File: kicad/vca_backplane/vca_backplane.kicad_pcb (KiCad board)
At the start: 4 copper layers, 147.2 x 109.9 mm, 102 parts, among them J1 Conn_02x20_Odd_Even, J10 AudioJack3DPDT, J2 Eurorack Power, J3 Conn_02x20_Odd_Even, J4 Conn_02x20_Odd_Even, J5 Conn_02x20_Odd_Even, J6 Conn_02x20_Odd_Even, J7 Conn_02x20_Odd_Even, J8 Conn_02x20_Odd_Even, J9 AudioJack3DPDT, Q1 DMMT5401, Q2 DMG2305UX, Q3 BSS138, Q4 BSS138, U1 74HCT138, U10 NE5532, U11 74HCT138, U12 MAX333A, U13 MAX333A, U14 NE5532, U2 74HCT245, U3 74LVC245, U4 MCP4822, U5 PCA9555PW, U7 AS3360, U8 M24C02-WMN, U9 PS508

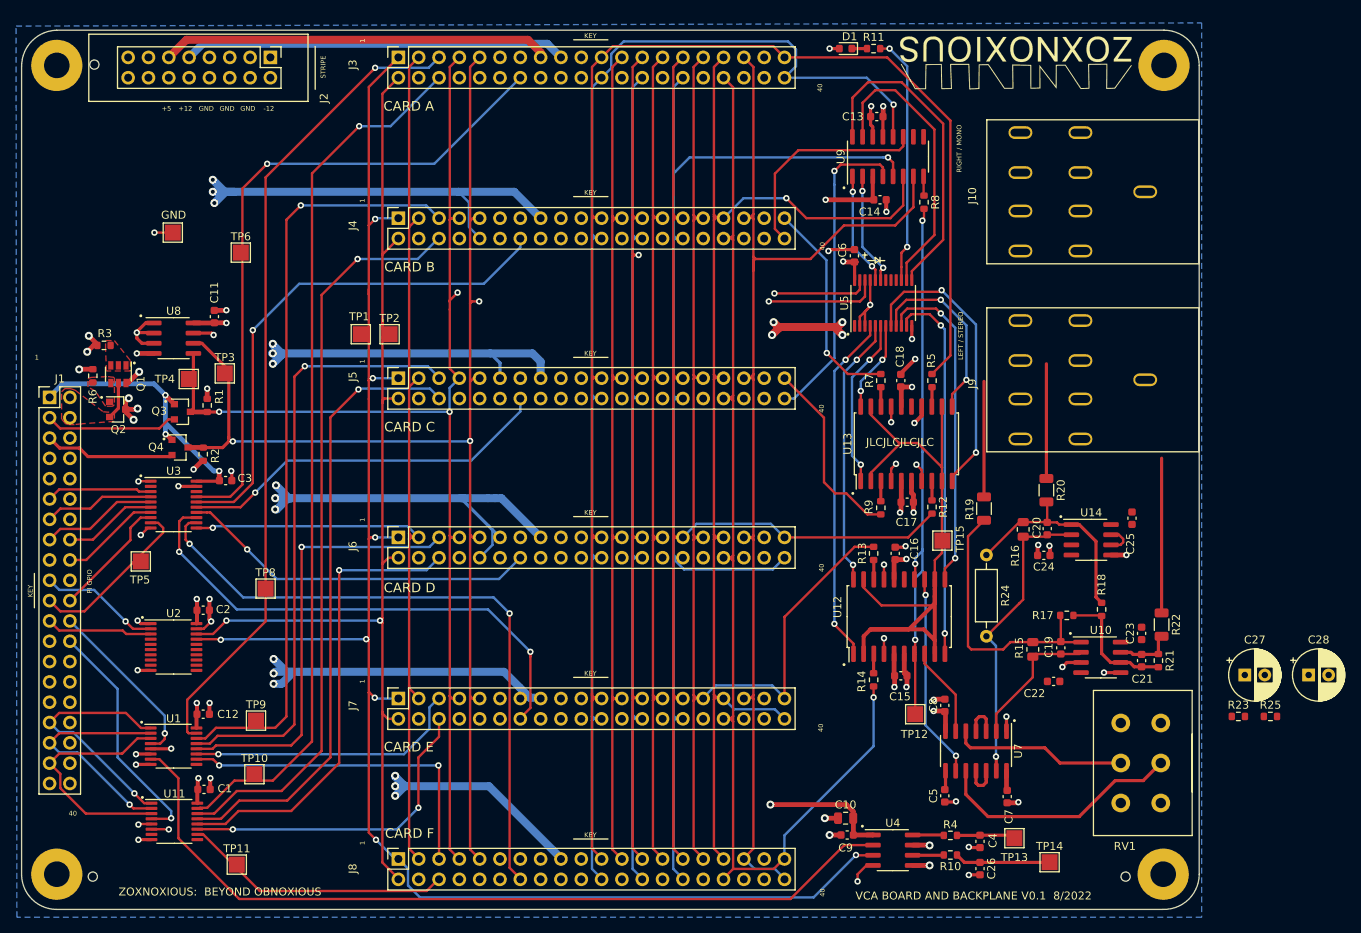
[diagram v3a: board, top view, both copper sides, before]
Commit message: fix some poor routing
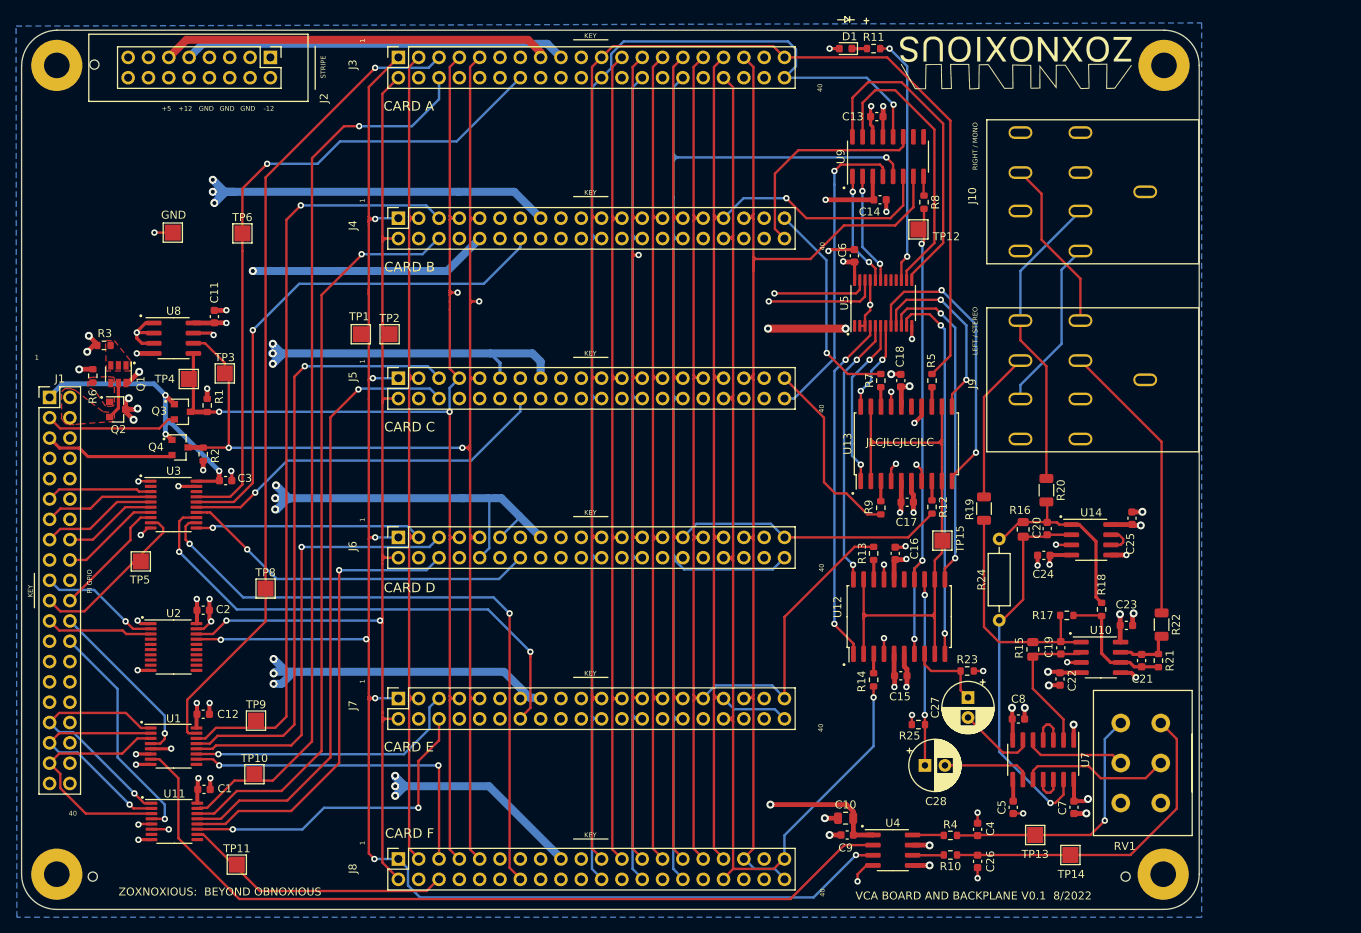
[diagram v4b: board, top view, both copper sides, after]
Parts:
- moved TP12 60.6 mm to (142.0, 58.3)
- moved C28 49.3 mm to (142.8, 125.3)
- moved R25 44.0 mm to (142.0, 120.2), turned to 180 degrees
- moved C27 34.7 mm to (148.2, 116.8), turned to -90 degrees
- moved R23 34.4 mm to (148.1, 113.5)
- moved C8 9.36 mm to (154.5, 119.5), turned to 0 degrees
- moved C5 8.67 mm to (153.8, 130.5)
- moved U7 8.47 mm to (157.6, 124.6)
- moved C7 8.46 mm to (161.4, 130.5)
- moved TP14 2.75 mm to (161.0, 136.5)
- moved TP13 2.63 mm to (156.6, 134.0)
- moved R24 2.56 mm to (152.1, 97.0)
- moved TP6 2.41 mm to (57.5, 58.8)
- moved C23 2.15 mm to (168.0, 107.8), turned to 0 degrees
- moved C4 1.53 mm to (149.4, 133.3)
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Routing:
- net +12V: track 340.2 -> 411.6 mm, vias 10 -> 11
- net -12V: track 381.4 -> 424.2 mm, vias 5 -> 6
- net Net-(C26-Pad2): track 13.4 -> 41.4 mm, vias 1 -> 0
- net +5V: track 458.8 -> 484.4 mm, vias 30 -> 31
- net /Sheet624DD88D/RIGHT: track 14.3 -> 38.0 mm
- net Net-(C4-Pad1): track 8.86 -> 32.3 mm
- net Net-(U12-Pad13): track 0.00 -> 23.3 mm, vias 0 -> 2
- net Net-(J10-Pad8): track 0.00 -> 21.6 mm
- net Net-(J10-Pad2): track 0.00 -> 21.6 mm
- net /Sheet624DD88D/MONO: track 19.3 -> 35.7 mm
- net Net-(U7-Pad9): track 25.6 -> 11.1 mm, vias 2 -> 0
- net /Sheet624DD88D/MIX1_VCA_IN: track 86.2 -> 71.9 mm
- net /Sheet624DD88D/DAC_CV_VCA_RIGHT: track 31.2 -> 18.7 mm
- net Net-(U12-Pad8): track 0.00 -> 9.87 mm
- net Net-(C20-Pad1): track 37.9 -> 47.6 mm
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
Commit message: getting to v0.2 for backplane
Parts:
- removed R24: DNP, Resistor_THT:R_Axial_DIN0207_L6.3mm_D2.5mm_P10.16mm_Horizontal
- R23, R25: footprint Resistor_SMD:R_0603_1608Metric -> Resistor_SMD:R_1206_3216Metric
- moved R19 3.45 mm to (151.9, 96.2)
- moved R23 1.55 mm to (149.6, 113.1)
- moved R25 0.89 mm to (141.2, 120.6)
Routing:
- net +5V: track 484.4 -> 427.4 mm, vias 31 -> 29
- net GND: track 1068.9 -> 1048.3 mm, vias 54 -> 74
- net +12V: track 411.6 -> 395.8 mm
- net Net-(C19-Pad2): track 30.1 -> 24.4 mm
- net Net-(C20-Pad2): track 24.7 -> 20.9 mm
- net /Sheet624DD88D/MIX1_VCA_IN: track 71.9 -> 68.7 mm
- net Net-(C20-Pad1): track 47.6 -> 44.8 mm, vias 1 -> 2
- net /Sheet624DD88D/LEFT: track 18.9 -> 21.2 mm
- net Net-(C27-Pad1): track 9.87 -> 10.5 mm
- added copper zone on B.Cu, net +12V
- added copper zone on B.Cu, net +5V
- added copper zone on F.Cu, net +5V
- added copper zone on F.Cu, net GND

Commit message: v0.2 of backplane submitted to jlcpcb
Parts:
- added R24: 10k, Resistor_SMD:R_0603_1608Metric, F.Cu at (42.0, 110.8)
- added R26: 10k, Resistor_SMD:R_0603_1608Metric, F.Cu at (42.0, 112.8)
- added R27: 10k, Resistor_SMD:R_0603_1608Metric, F.Cu at (45.3, 87.6)
- added R28: 10k, Resistor_SMD:R_0603_1608Metric, F.Cu at (47.4, 116.1)
- added R29: 10k, Resistor_SMD:R_0603_1608Metric, F.Cu at (49.4, 116.1)
- R10, R4: value 12k -> 10k
- moved G*** 121.1 mm to (34.7, 57.3), turned to -90 degrees
- moved C28 5.92 mm to (148.1, 128.0), turned to 90 degrees
- moved D1 4.83 mm to (137.7, 35.2)
- moved R11 4.83 mm to (141.2, 35.2)
- moved C12 1.20 mm to (51.8, 118.0), turned to -90 degrees
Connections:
- J3 pad 1: /SPI_CLK_5V -> /SPI_CLK1_5V
- J3 pad 2: /SPI_MOSI_5V -> /SPI_MOSI1_5V
- J4 pad 1: /SPI_CLK_5V -> /SPI_CLK1_5V
- J4 pad 2: /SPI_MOSI_5V -> /SPI_MOSI1_5V
- J5 pad 1: /SPI_CLK_5V -> /SPI_CLK1_5V
- J5 pad 2: /SPI_MOSI_5V -> /SPI_MOSI1_5V
- J6 pad 1: /SPI_CLK_5V -> /SPI_CLK1_5V
- J6 pad 2: /SPI_MOSI_5V -> /SPI_MOSI1_5V
- J7 pad 1: /SPI_CLK_5V -> /SPI_CLK2_5V
- J7 pad 2: /SPI_MOSI_5V -> /SPI_MOSI2_5V
- J8 pad 1: /SPI_CLK_5V -> /SPI_CLK2_5V
- J8 pad 2: /SPI_MOSI_5V -> /SPI_MOSI2_5V
- TP1 pad 1: /SPI_CLK_5V -> /SPI_CLK1_5V
- TP2 pad 1: /SPI_MOSI_5V -> /SPI_MOSI1_5V
- U2 pad 15: unconnected-(U2-Pad15) -> /SPI_MOSI2_5V
- U2 pad 16: unconnected-(U2-Pad16) -> /SPI_CLK2_5V
- U2 pad 17: /SPI_CLK_5V -> /SPI_CLK1_5V
- U2 pad 18: /SPI_MOSI_5V -> /SPI_MOSI1_5V
- U2 pad 4: unconnected-(U2-Pad4) -> /SPI_CLK
- U2 pad 5: unconnected-(U2-Pad5) -> /SPI_MOSI
- U2 pad 6: unconnected-(U2-Pad6) -> Net-(R24-Pad2)
- U2 pad 7: unconnected-(U2-Pad7) -> Net-(R26-Pad2)
- U2 pad 8: unconnected-(U2-Pad8) -> Net-(R29-Pad2)
- U2 pad 9: unconnected-(U2-Pad9) -> Net-(R28-Pad2)
- U3 pad 2: unconnected-(U3-Pad2) -> Net-(R27-Pad1)
- U4 pad 3: /SPI_CLK_5V -> /SPI_CLK2_5V
- U4 pad 4: /SPI_MOSI_5V -> /SPI_MOSI2_5V
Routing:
- net /SPI_CLK_5V: track 210.7 -> 0.00 mm, vias 8 -> 0
- net /SPI_MOSI_5V: track 201.1 -> 0.00 mm, vias 3 -> 0
- net /SPI_CLK2_5V: track 0.00 -> 114.0 mm, vias 0 -> 3
- net /SPI_MOSI2_5V: track 0.00 -> 113.3 mm, vias 0 -> 3
- net /SPI_CLK1_5V: track 0.00 -> 108.7 mm, vias 0 -> 5
- net /SPI_MOSI1_5V: track 0.00 -> 102.8 mm, vias 0 -> 2
- net +5V: track 427.4 -> 436.9 mm
- net GND: track 1048.3 -> 1055.0 mm, vias 74 -> 91
- net /SPI_CS0_F: track 42.2 -> 35.5 mm, vias 2 -> 1
- net Net-(C28-Pad1): track 23.4 -> 29.8 mm
- net Net-(R29-Pad2): track 0.00 -> 5.77 mm
- net Net-(R27-Pad1): track 0.00 -> 4.65 mm
- net /SPI_CS1_E: track 41.1 -> 36.7 mm, vias 2 -> 1
- net /SPI_MOSI: track 15.1 -> 19.4 mm
- net Net-(R26-Pad2): track 0.00 -> 3.76 mm
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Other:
- board text added: "VCA / BACKPLANE V0.2 9/2022"
- board text removed: "VCA BOARD AND BACKPLANE V0.1 8/2022"
